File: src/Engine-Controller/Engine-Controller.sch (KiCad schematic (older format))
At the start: 5 parts, among them U1 STM32L443VCT6

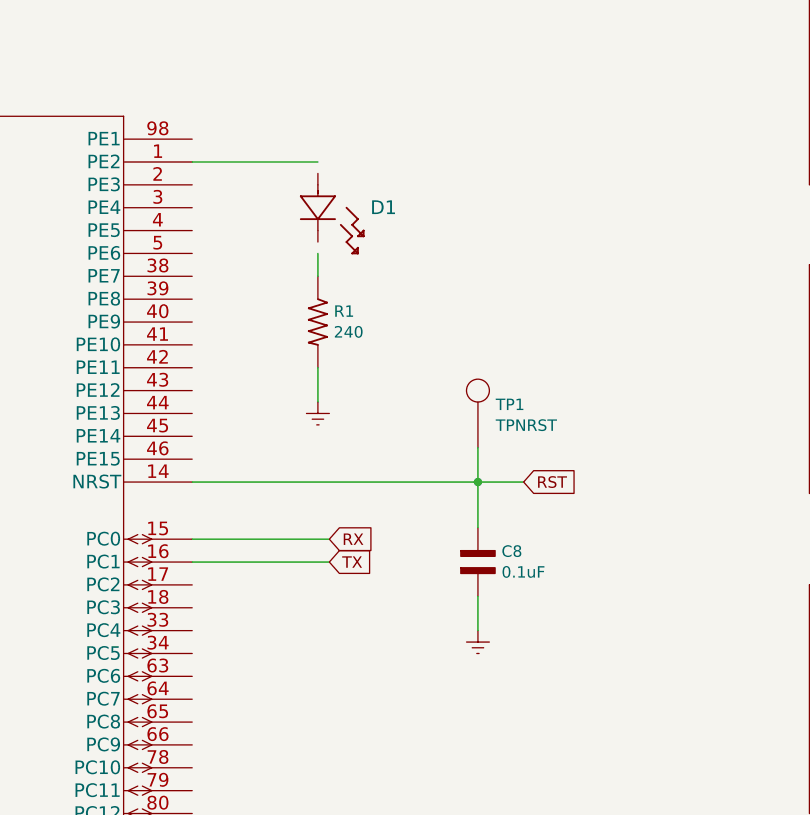
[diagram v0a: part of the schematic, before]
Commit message: Updated Connector pinouts and added button to Reset pin
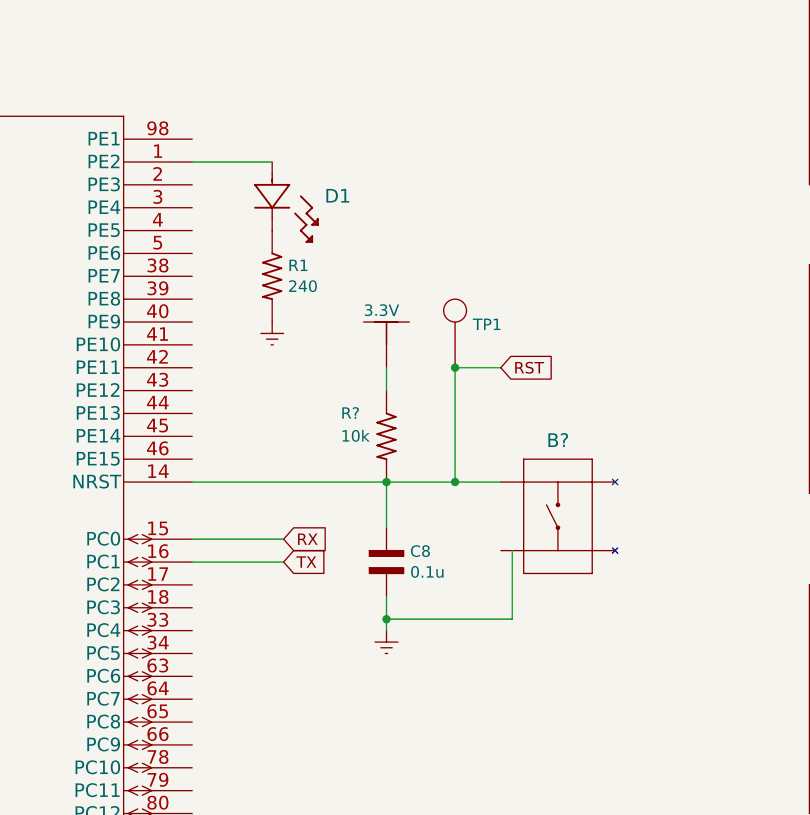
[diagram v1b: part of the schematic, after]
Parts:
- added B?: PTS647SM38SMTR2LFS, SW_PTS647SM38SMTR2LFS_CNK, symbol Engine-Controller:PTS647SM38SMTR2LFS
- added None?: 3.3V, symbol Engine-Controller:3.3V
- added R?: 10k, symbol Engine-Controller:RES_0603
- C8: value 0.1uF -> 0.1u
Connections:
- wire segments 56 -> 60
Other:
- moved on the sheet: C8, D1, R1, TP1
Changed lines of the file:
@@
 F1 "Connectors.sch" 50
 $EndSheet
-Text GLabel 6000 3350 2    50   Input ~ 0
+Text GLabel 5800 3350 2    50   Input ~ 0
 RX
-Text GLabel 6000 3450 2    50   Input ~ 0
+Text GLabel 5800 3450 2    50   Input ~ 0
 TX
 Text GLabel 2500 4050 0    50   Input ~ 0
@@
 SS
 Wire Wire Line
-	5400 3350 6000 3350
-Wire Wire Line
-	5400 3450 6000 3450
-Wire Wire Line
 	3000 3950 2500 3950
 Wire Wire Line
@@
 Text GLabel 2550 4650 0    50   Input ~ 0
 SWDIO
-Text GLabel 6850 3100 2    50   Input ~ 0
+Text GLabel 6750 2600 2    50   Input ~ 0
 RST
 Wire Wire Line
@@
 Wire Wire Line
 	3000 4750 2550 4750
-$Comp
-L Engine-Controller:150120AS75000 D1
-U 1 1 61009279
-P 5950 1950
-F 0 "D1" H 6179 2000 60  0000 L CNN
-F 1 "150120AS75000" H 6179 1947 60  0001 L CNN
-F 2 "Engine-Controller:150120AS75000" H 6150 1590 60  0001 C CNN
-F 3 "" V 5950 2200 60  0000 C CNN
-	1    5950 1950
-	1    0    0    -1
-$EndComp
-$Comp
-L Engine-Controller:RES_0603 R1
-U 1 1 6100A5B9
-P 5950 2400
-F 0 "R1" V 5904 2469 50  0000 L CNN
-F 1 "240" V 5995 2469 50  0000 L CNN
-F 2 "Engine-Controller:RES_0603" H 6000 1900 50  0001 L BNN
-F 3 "" H 5950 2400 50  0001 L BNN
-	1    5950 2400
-	0    1    1    0
-$EndComp
-Wire Wire Line
-	5400 1700 5950 1700
-Wire Wire Line
-	5950 2100 5950 2200
-$Comp
-L power:Earth #PWR0102
-U 1 1 6102ABA9
-P 5950 2750
-F 0 "#PWR0102" H 5950 2500 50  0001 C CNN
-F 1 "Earth" H 5950 2600 50  0001 C CNN
-F 2 "" H 5950 2750 50  0001 C CNN
-F 3 "~" H 5950 2750 50  0001 C CNN
-	1    5950 2750
-	1    0    0    -1
-$EndComp
-Wire Wire Line
-	5950 2600 5950 2750
 Text GLabel 6000 5100 2    50   Input ~ 0
 IO1
@@
 Text Label 2550 1450 0    50   ~ 0
 3.3V
-Wire Wire Line
-	5400 3100 6650 3100
 $Comp
 L Engine-Controller:CAP_0603 C8
 U 1 1 60DE014C
-P 6650 3450
-F 0 "C8" V 6604 3553 50  0000 L CNN
-F 1 "0.1uF" V 6695 3553 50  0000 L CNN
-F 2 "Engine-Controller:CAP_0603" H 6550 3050 50  0001 L BNN
-F 3 "" H 6600 3450 50  0001 L BNN
-	1    6650 3450
+P 6250 3450
+F 0 "C8" V 6204 3553 50  0000 L CNN
+F 1 "0.1u" V 6295 3553 50  0000 L CNN
+F 2 "Engine-Controller:CAP_0603" H 6150 3050 50  0001 L BNN
+F 3 "" H 6200 3450 50  0001 L BNN
+	1    6250 3450
 	0    1    1    0
 $EndComp
@@
 L power:Earth #PWR01
 U 1 1 60DE602C
-P 6650 3750
-F 0 "#PWR01" H 6650 3500 50  0001 C CNN
-F 1 "Earth" H 6650 3600 50  0001 C CNN
-F 2 "" H 6650 3750 50  0001 C CNN
-F 3 "~" H 6650 3750 50  0001 C CNN
-	1    6650 3750
-	1    0    0    -1
-$EndComp
-Wire Wire Line
-	6650 3300 6650 3100
-Connection ~ 6650 3100
-Wire Wire Line
-	6650 3100 6850 3100
-Wire Wire Line
-	6650 3750 6650 3600
+P 6250 3750
+F 0 "#PWR01" H 6250 3500 50  0001 C CNN
+F 1 "Earth" H 6250 3600 50  0001 C CNN
+F 2 "" H 6250 3750 50  0001 C CNN
+F 3 "~" H 6250 3750 50  0001 C CNN
+	1    6250 3750
+	1    0    0    -1
+$EndComp
+Wire Wire Line
+	6250 3300 6250 3100
+Wire Wire Line
+	6250 3750 6250 3700
 $Comp
 L Engine-Controller:TP TP1
 U 1 1 60E1CD7C
-P 6650 2950
-F 0 "TP1" H 6728 3138 50  0000 L CNN
-F 1 "TPNRST" H 6728 3047 50  0000 L CNN
-F 2 "Engine-Controller:TP" H 6650 2950 50  0001 C CNN
-F 3 "" H 6650 2950 50  0001 C CNN
-	1    6650 2950
-	1    0    0    -1
-$EndComp
-Wire Wire Line
-	6650 3100 6650 2950
+P 6550 2600
+F 0 "TP1" H 6628 2788 50  0000 L CNN
+F 1 "TPNRST" H 6628 2697 50  0001 L CNN
+F 2 "Engine-Controller:TP" H 6550 2600 50  0001 C CNN
+F 3 "" H 6550 2600 50  0001 C CNN
+	1    6550 2600
+	1    0    0    -1
+$EndComp
+Wire Wire Line
+	5400 3350 5800 3350
+Wire Wire Line
+	5800 3450 5400 3450
+$Comp
+L power:Earth #PWR0102
+U 1 1 6102ABA9
+P 5750 2400
+F 0 "#PWR0102" H 5750 2150 50  0001 C CNN
+F 1 "Earth" H 5750 2250 50  0001 C CNN
+F 2 "" H 5750 2400 50  0001 C CNN
+F 3 "~" H 5750 2400 50  0001 C CNN
+	1    5750 2400
+	1    0    0    -1
+$EndComp
+$Comp
+L Engine-Controller:RES_0603 R1
+U 1 1 6100A5B9
+P 5750 2200
+F 0 "R1" V 5704 2269 50  0000 L CNN
+F 1 "240" V 5795 2269 50  0000 L CNN
+F 2 "Engine-Controller:RES_0603" H 5800 1700 50  0001 L BNN
+F 3 "" H 5750 2200 50  0001 L BNN
+	1    5750 2200
+	0    1    1    0
+$EndComp
+$Comp
+L Engine-Controller:150120AS75000 D1
+U 1 1 61009279
+P 5750 1900
+F 0 "D1" H 5979 1950 60  0000 L CNN
+F 1 "150120AS75000" H 5979 1897 60  0001 L CNN
+F 2 "Engine-Controller:150120AS75000" H 5950 1540 60  0001 C CNN
+F 3 "" V 5750 2150 60  0000 C CNN
+	1    5750 1900
+	1    0    0    -1
+$EndComp
+Wire Wire Line
+	5400 1700 5750 1700
+$Comp
+L Engine-Controller:PTS647SM38SMTR2LFS B?
+U 1 1 610156A4
+P 7000 3250
+F 0 "B?" H 7000 3581 60  0000 C CNN
+F 1 "PTS647SM38SMTR2LFS" H 7000 3581 60  0001 C CNN
+F 2 "SW_PTS647SM38SMTR2LFS_CNK" H 7000 2800 60  0001 C CNN
+F 3 "" H 6200 3400 60  0001 C CNN
+	1    7000 3250
+	1    0    0    -1
+$EndComp
+Wire Wire Line
+	6250 2700 6250 2600
+$Comp
+L Engine-Controller:RES_0603 R?
+U 1 1 60FC75D6
+P 6250 2900
+F 0 "R?" V 6150 2700 50  0000 L CNN
+F 1 "10k" V 6250 2700 50  0000 L CNN
+F 2 "" H 6300 2400 50  0001 L BNN
+F 3 "" H 6250 2900 50  0001 L BNN
+	1    6250 2900
+	0    1    1    0
+$EndComp
+$Comp
+L Engine-Controller:3.3V None?
+U 1 1 60F82434
+P 6250 2450
+F 0 "None?" H 6378 2439 50  0001 L CNN
+F 1 "3.3V" H 6150 2550 50  0000 L CNN
+F 2 "" H 6250 2450 50  0001 C CNN
+F 3 "" H 6250 2450 50  0001 C CNN
+	1    6250 2450
+	1    0    0    -1
+$EndComp
+Connection ~ 6250 3100
+Wire Wire Line
+	5400 3100 6250 3100
+Wire Wire Line
+	6250 3100 6550 3100
+Wire Wire Line
+	6550 2600 6550 3100
+Connection ~ 6550 3100
+Wire Wire Line
+	6550 3100 6750 3100
+Wire Wire Line
+	6750 2600 6550 2600
+Connection ~ 6550 2600
+Wire Wire Line
+	6800 3400 6800 3700
+Wire Wire Line
+	6800 3700 6250 3700
+Connection ~ 6250 3700
+Wire Wire Line
+	6250 3700 6250 3600
 $EndSCHEMATC

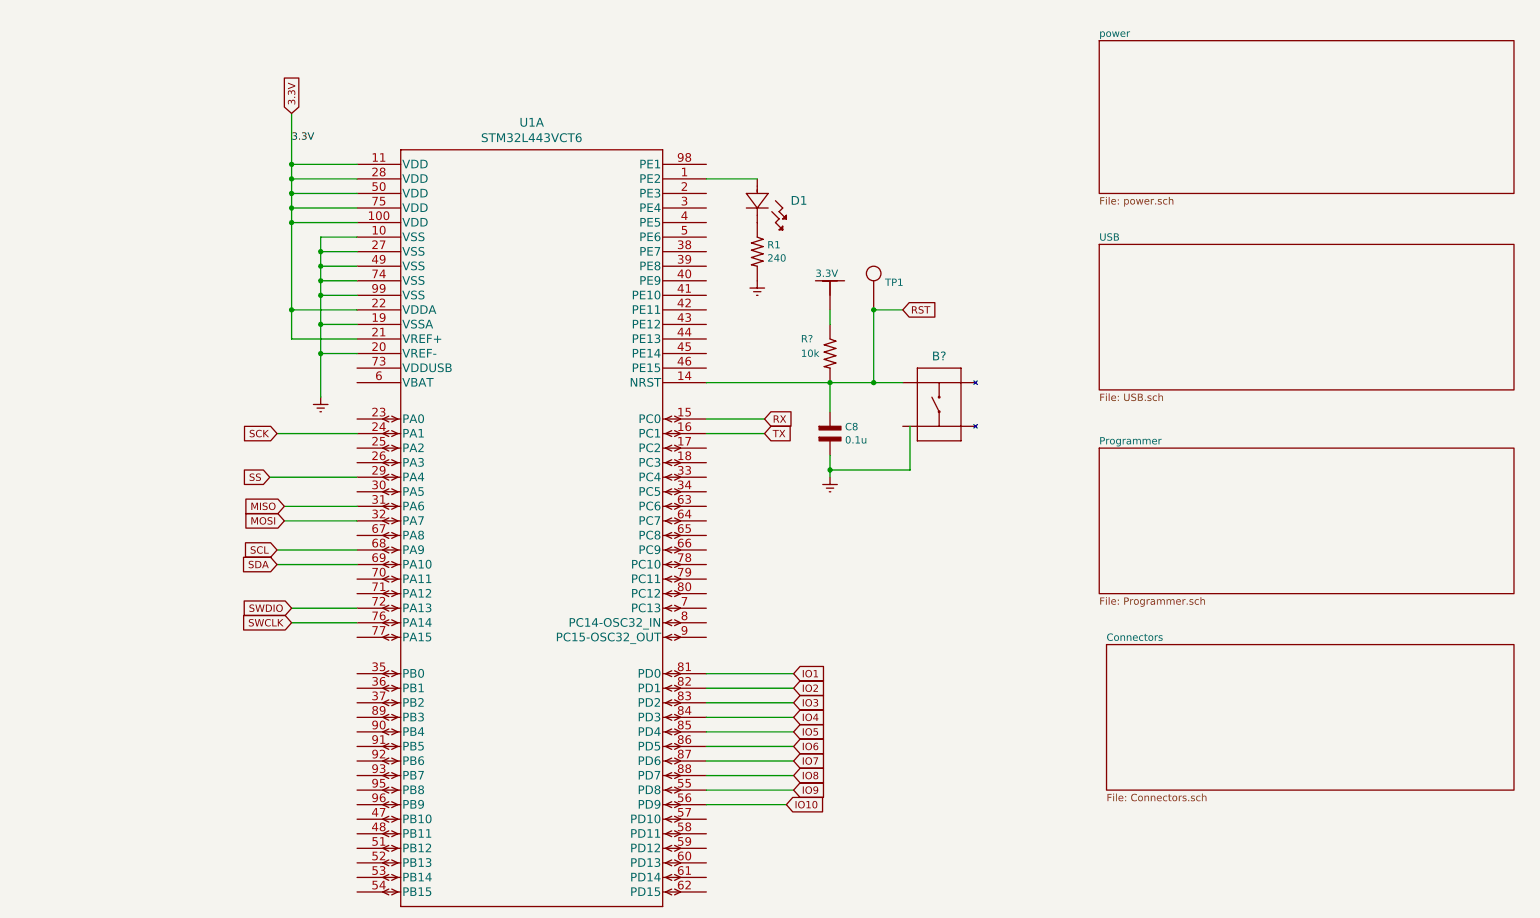
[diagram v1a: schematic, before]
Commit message: Added buffer to some IOs
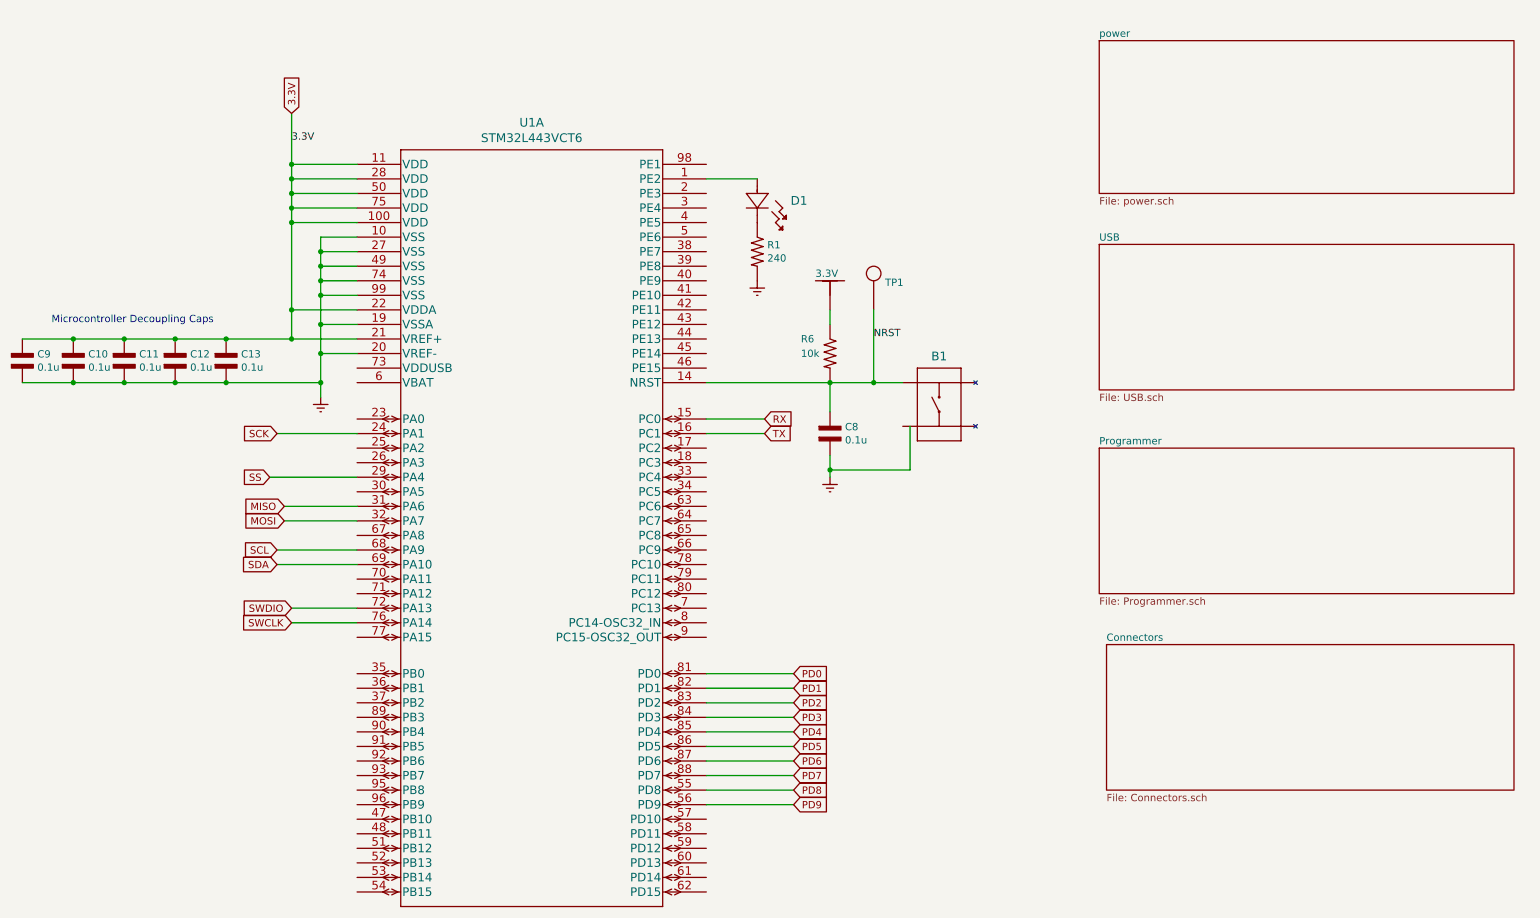
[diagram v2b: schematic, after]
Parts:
- added C10, C11, C12, C13, C9: 0.1u, symbol Engine-Controller:CAP_0603
- gave numbers to parts that had none: 3
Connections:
- net 3.3V: now also C10.2, C11.2, C12.2, C13.2, C9.2
- net Earth: now also C10.1, C11.1, C12.1, C13.1, C9.1
- net IO1 renamed PD0
- net IO10 renamed PD9
- net IO2 renamed PD1
- net IO3 renamed PD2
- net IO4 renamed PD3
- net IO5 renamed PD4
- net IO6 renamed PD5
- net IO7 renamed PD6
- net IO8 renamed PD7
- net IO9 renamed PD8
- net RST renamed NRST
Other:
- note added: "Microcontroller Decoupling Caps"
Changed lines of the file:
@@
 	3000 2900 2750 2900
 Wire Wire Line
-	2750 2900 2750 3200
+	2750 2900 2750 3100
 Wire Wire Line
 	3000 2700 2750 2700
@@
 Text GLabel 2550 4650 0    50   Input ~ 0
 SWDIO
-Text GLabel 6750 2600 2    50   Input ~ 0
-RST
 Wire Wire Line
 	3000 4650 2550 4650
@@
 	3000 4750 2550 4750
 Text GLabel 6000 5100 2    50   Input ~ 0
-IO1
+PD0
 Text GLabel 6000 5200 2    50   Input ~ 0
-IO2
+PD1
 Text GLabel 6000 5300 2    50   Input ~ 0
-IO3
+PD2
 Text GLabel 6000 5400 2    50   Input ~ 0
-IO4
+PD3
 Text GLabel 6000 5500 2    50   Input ~ 0
-IO5
+PD4
 Text GLabel 6000 5600 2    50   Input ~ 0
-IO6
+PD5
 Text GLabel 6000 5700 2    50   Input ~ 0
-IO7
+PD6
 Text GLabel 6000 5800 2    50   Input ~ 0
-IO8
+PD7
 Text GLabel 6000 5900 2    50   Input ~ 0
-IO9
-Text GLabel 5950 6000 2    50   Input ~ 0
-IO10
+PD8
+Text GLabel 6000 6000 2    50   Input ~ 0
+PD9
 Wire Wire Line
 	6000 5100 5400 5100
@@
 Wire Wire Line
 	6000 5900 5400 5900
-Wire Wire Line
-	5950 6000 5400 6000
 Text Label 2550 1450 0    50   ~ 0
 3.3V
@@
 	5400 1700 5750 1700
 $Comp
-L Engine-Controller:PTS647SM38SMTR2LFS B?
+L Engine-Controller:PTS647SM38SMTR2LFS B1
 U 1 1 610156A4
 P 7000 3250
-F 0 "B?" H 7000 3581 60  0000 C CNN
+F 0 "B1" H 7000 3581 60  0000 C CNN
 F 1 "PTS647SM38SMTR2LFS" H 7000 3581 60  0001 C CNN
 F 2 "SW_PTS647SM38SMTR2LFS_CNK" H 7000 2800 60  0001 C CNN
@@
 	6250 2700 6250 2600
 $Comp
-L Engine-Controller:RES_0603 R?
+L Engine-Controller:RES_0603 R6
 U 1 1 60FC75D6
 P 6250 2900
-F 0 "R?" V 6150 2700 50  0000 L CNN
+F 0 "R6" V 6150 2700 50  0000 L CNN
 F 1 "10k" V 6250 2700 50  0000 L CNN
 F 2 "" H 6300 2400 50  0001 L BNN
@@
 $EndComp
 $Comp
-L Engine-Controller:3.3V None?
+L Engine-Controller:3.3V None01
 U 1 1 60F82434
 P 6250 2450
-F 0 "None?" H 6378 2439 50  0001 L CNN
+F 0 "None01" H 6378 2439 50  0001 L CNN
 F 1 "3.3V" H 6150 2550 50  0000 L CNN
 F 2 "" H 6250 2450 50  0001 C CNN
@@
 	6550 3100 6750 3100
 Wire Wire Line
-	6750 2600 6550 2600
-Connection ~ 6550 2600
-Wire Wire Line
 	6800 3400 6800 3700
 Wire Wire Line
@@
 Wire Wire Line
 	6250 3700 6250 3600
+$Comp
+L Engine-Controller:CAP_0603 C10
+U 1 1 61273C95
+P 1050 2950
+F 0 "C10" V 1004 3053 50  0000 L CNN
+F 1 "0.1u" V 1095 3053 50  0000 L CNN
+F 2 "" H 950 2550 50  0001 L BNN
+F 3 "" H 1000 2950 50  0001 L BNN
+	1    1050 2950
+	0    1    1    0
+$EndComp
+$Comp
+L Engine-Controller:CAP_0603 C11
+U 1 1 6127C459
+P 1400 2950
+F 0 "C11" V 1354 3053 50  0000 L CNN
+F 1 "0.1u" V 1445 3053 50  0000 L CNN
+F 2 "" H 1300 2550 50  0001 L BNN
+F 3 "" H 1350 2950 50  0001 L BNN
+	1    1400 2950
+	0    1    1    0
+$EndComp
+$Comp
+L Engine-Controller:CAP_0603 C12
+U 1 1 6127D073
+P 1750 2950
+F 0 "C12" V 1704 3053 50  0000 L CNN
+F 1 "0.1u" V 1795 3053 50  0000 L CNN
+F 2 "" H 1650 2550 50  0001 L BNN
+F 3 "" H 1700 2950 50  0001 L BNN
+	1    1750 2950
+	0    1    1    0
+$EndComp
+$Comp
+L Engine-Controller:CAP_0603 C13
+U 1 1 6127DC78
+P 2100 2950
+F 0 "C13" V 2054 3053 50  0000 L CNN
+F 1 "0.1u" V 2145 3053 50  0000 L CNN
+F 2 "" H 2000 2550 50  0001 L BNN
+F 3 "" H 2050 2950 50  0001 L BNN
+	1    2100 2950
+	0    1    1    0
+$EndComp
+$Comp
+L Engine-Controller:CAP_0603 C9
+U 1 1 6127EE14
+P 700 2950
+F 0 "C9" V 654 3053 50  0000 L CNN
+F 1 "0.1u" V 745 3053 50  0000 L CNN
+F 2 "" H 600 2550 50  0001 L BNN
+F 3 "" H 650 2950 50  0001 L BNN
+	1    700  2950
+	0    1    1    0
+$EndComp
+Wire Wire Line
+	2550 2800 2100 2800
+Connection ~ 2550 2800
+Connection ~ 1050 2800
+Wire Wire Line
+	1050 2800 700  2800
+Connection ~ 1400 2800
+Wire Wire Line
+	1400 2800 1050 2800
+Connection ~ 1750 2800
+Wire Wire Line
+	1750 2800 1400 2800
+Connection ~ 2100 2800
+Wire Wire Line
+	2100 2800 1750 2800
+Wire Wire Line
+	700  3100 1050 3100
+Connection ~ 2750 3100
+Wire Wire Line
+	2750 3100 2750 3200
+Connection ~ 1050 3100
+Wire Wire Line
+	1050 3100 1400 3100
+Connection ~ 1400 3100
+Wire Wire Line
+	1400 3100 1750 3100
+Connection ~ 1750 3100
+Wire Wire Line
+	1750 3100 2100 3100
+Connection ~ 2100 3100
+Wire Wire Line
+	2100 3100 2750 3100
+Text Notes 900  2700 0    50   ~ 0
+Microcontroller Decoupling Caps
+Text Label 6550 2800 0    50   ~ 0
+NRST
+Wire Wire Line
+	5400 6000 6000 6000
 $EndSCHEMATC

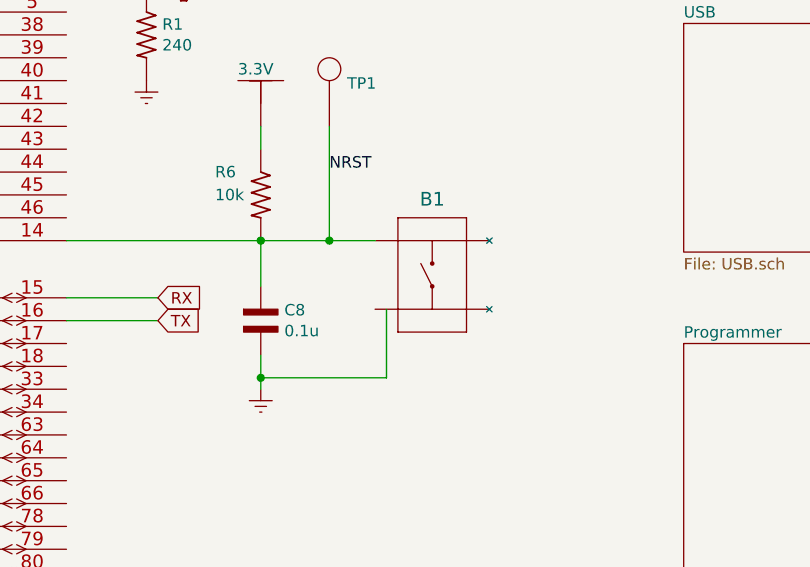
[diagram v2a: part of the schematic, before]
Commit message: Added NO Jumper to NRST button
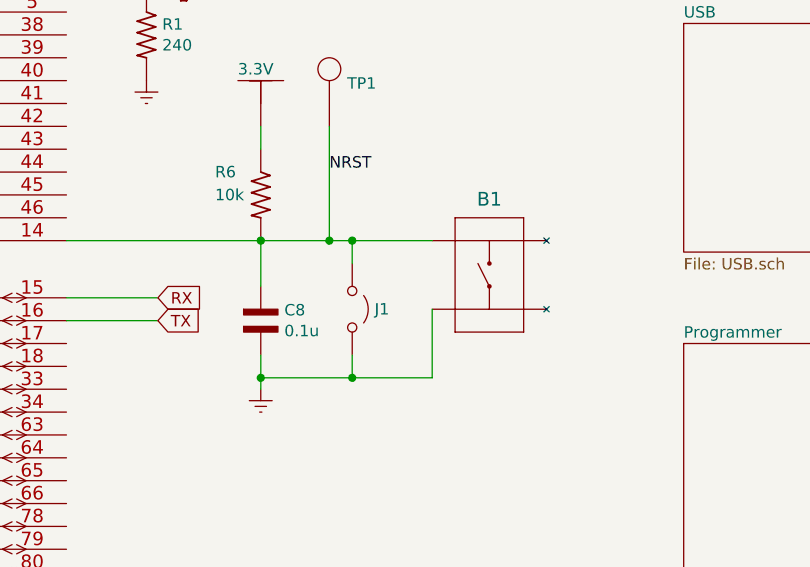
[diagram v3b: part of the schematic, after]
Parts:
- added J1: Jumper_NO, symbol Engine-Controller:Jumper_NO
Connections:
- net Earth: now also B1.3, J1.2 (B)
- net NRST: now also J1.1 (A)
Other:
- moved on the sheet: B1
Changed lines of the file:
@@
 L Engine-Controller:PTS647SM38SMTR2LFS B1
 U 1 1 610156A4
-P 7000 3250
-F 0 "B1" H 7000 3581 60  0000 C CNN
-F 1 "PTS647SM38SMTR2LFS" H 7000 3581 60  0001 C CNN
-F 2 "SW_PTS647SM38SMTR2LFS_CNK" H 7000 2800 60  0001 C CNN
-F 3 "" H 6200 3400 60  0001 C CNN
-	1    7000 3250
+P 7250 3250
+F 0 "B1" H 7250 3581 60  0000 C CNN
+F 1 "PTS647SM38SMTR2LFS" H 7250 3581 60  0001 C CNN
+F 2 "SW_PTS647SM38SMTR2LFS_CNK" H 7250 2800 60  0001 C CNN
+F 3 "" H 6450 3400 60  0001 C CNN
+	1    7250 3250
 	1    0    0    -1
 $EndComp
@@
 Connection ~ 6550 3100
 Wire Wire Line
-	6550 3100 6750 3100
-Wire Wire Line
-	6800 3400 6800 3700
-Wire Wire Line
-	6800 3700 6250 3700
+	6550 3100 6650 3100
 Connection ~ 6250 3700
 Wire Wire Line
@@
 Wire Wire Line
 	5400 6000 6000 6000
+$Comp
+L Engine-Controller:Jumper_NO J1
+U 1 1 6147D8EA
+P 6650 3400
+F 0 "J1" V 6650 3498 50  0000 L CNN
+F 1 "Jumper_NO" H 6650 3310 50  0001 C CNN
+F 2 "" H 6650 3400 50  0001 C CNN
+F 3 "~" H 6650 3400 50  0001 C CNN
+	1    6650 3400
+	0    1    1    0
+$EndComp
+Wire Wire Line
+	6650 3200 6650 3100
+Connection ~ 6650 3100
+Wire Wire Line
+	6650 3600 6650 3700
+Connection ~ 6650 3700
+Wire Wire Line
+	6650 3700 6250 3700
+Wire Wire Line
+	6650 3100 7000 3100
+Wire Wire Line
+	7000 3700 7000 3400
+Wire Wire Line
+	6650 3700 7000 3700
 $EndSCHEMATC
